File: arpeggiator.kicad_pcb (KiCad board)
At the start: 4 copper layers, 220 x 170 mm, 360 parts, among them J202 logic test header, J601 3.5mm mono line out, J701 PJ-102AH / 12V DC centre +, Q601 2N7002, Q602 MMBT3904, Q603 BSS84, Q604 MMBT3904, Q605 2N7002, Q606 MMBT3906, Q701 AO3401A, Q702 MMBT3906, Q703 MMBT3906, SW101 C, SW102 C sharp, SW103 D, SW104 D sharp, SW105 E, SW106 F, SW107 F sharp, SW108 G, SW109 G sharp, SW110 A, SW111 A sharp, SW112 B, SW113 start / stop, SW114 1 / 2 / 3 octaves, SW601 saw / pulse, U101 TLC555IDR, U102 TLC555IDR, U103 MCP100T-450I/TT, U201 74HC574, U202 74HC574, U203 74HC574, U204 74HC574, U205 74HC377, U206 74HC377, U211 74HC163, U212 74HC138, U213 74HC163, U214 74HC163, U215 74HC163, U216 CD74HC4067M, U221 74HC377, U222 74HC154, U301 74HC74, U302 74HC74, U303 74HC74, U401 74HC14, U402 74HC14, U403 74HC14, U404 74HC04, U405 74HC04, U406 74HC08, U407 74HC86, U408 74HC04, U409 74HC32, U410 74HC32, U411 74HC32, U412 74HC32, U413 74HC08, U414 74HC08, U415 74HC86, U416 74HC04, U417 74HC08, U418 74HC08, U419 74HC32, U420 74HC14, U421 74HC08, U422 74HC32, U423 74HC08, U424 74HC32, U425 74HC08, U501 OPA4192IDR, U502 ADG706BRUZ, U503 74HC4051D, U504 AS3340A, U601 TLC555IDR, U602 OPA4192IDR, U603 TL074HIDR, U604 LM13700M/NOPB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

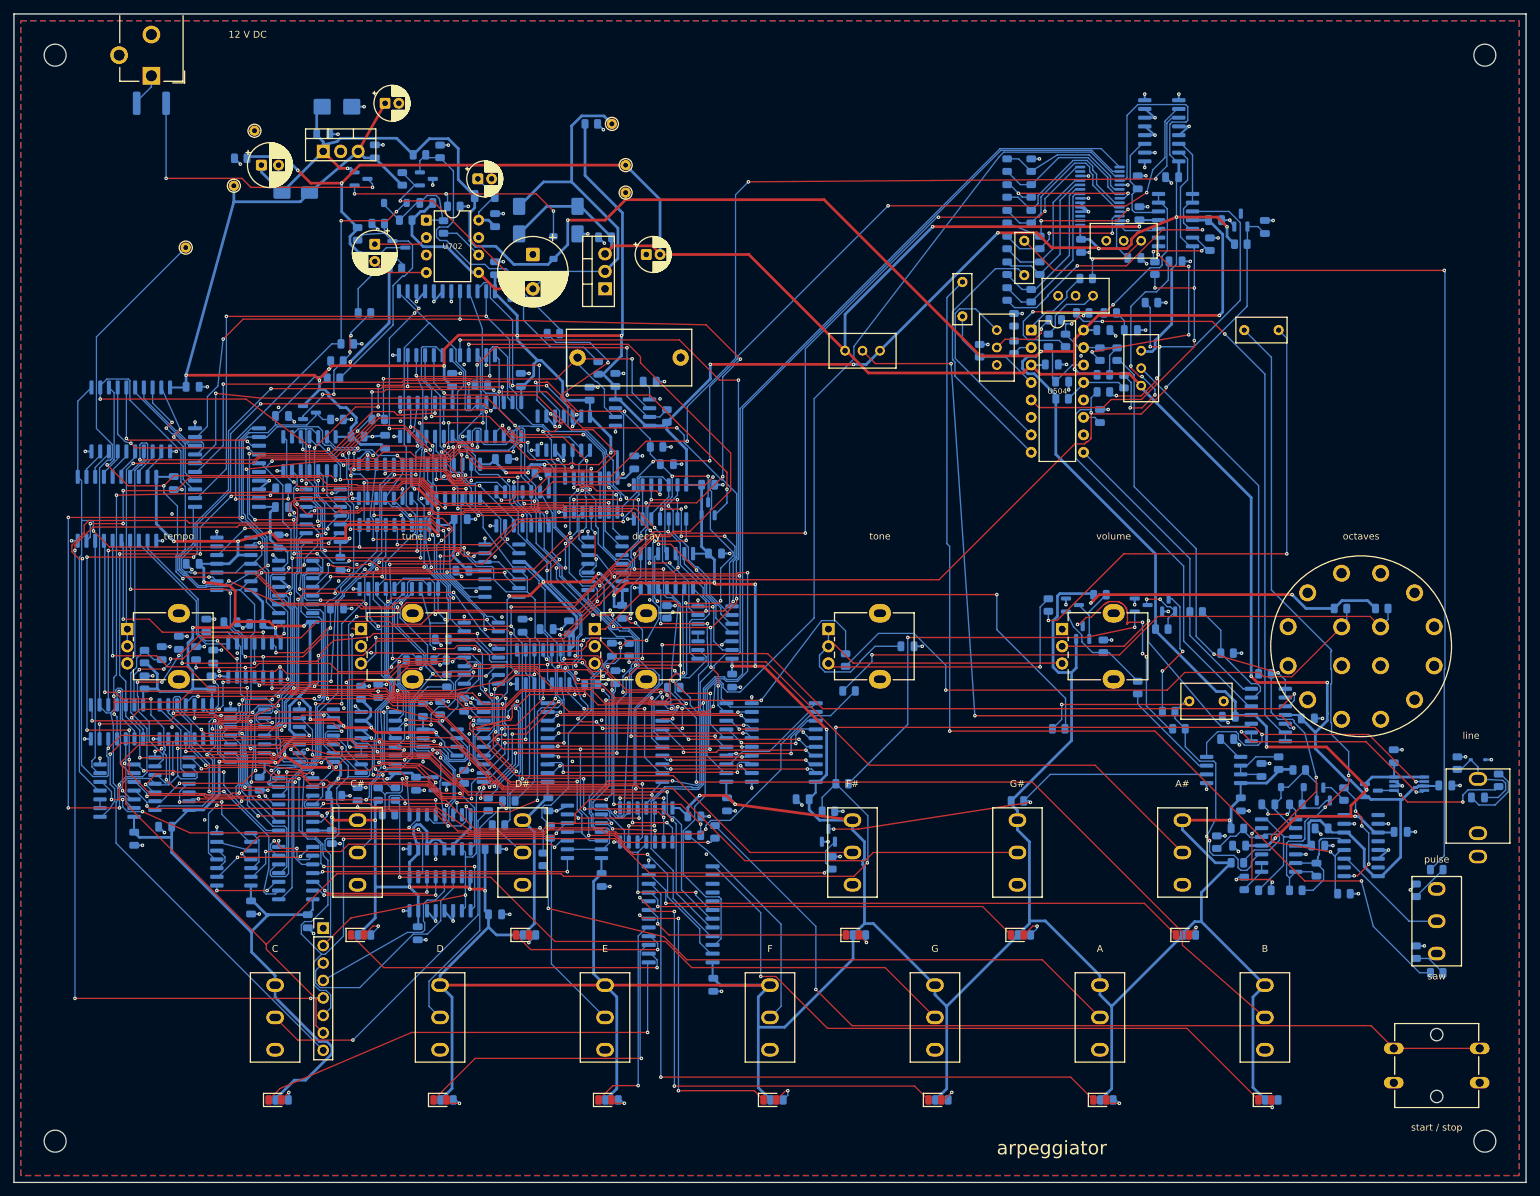
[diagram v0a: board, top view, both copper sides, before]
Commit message: parts and cheaper PCB files
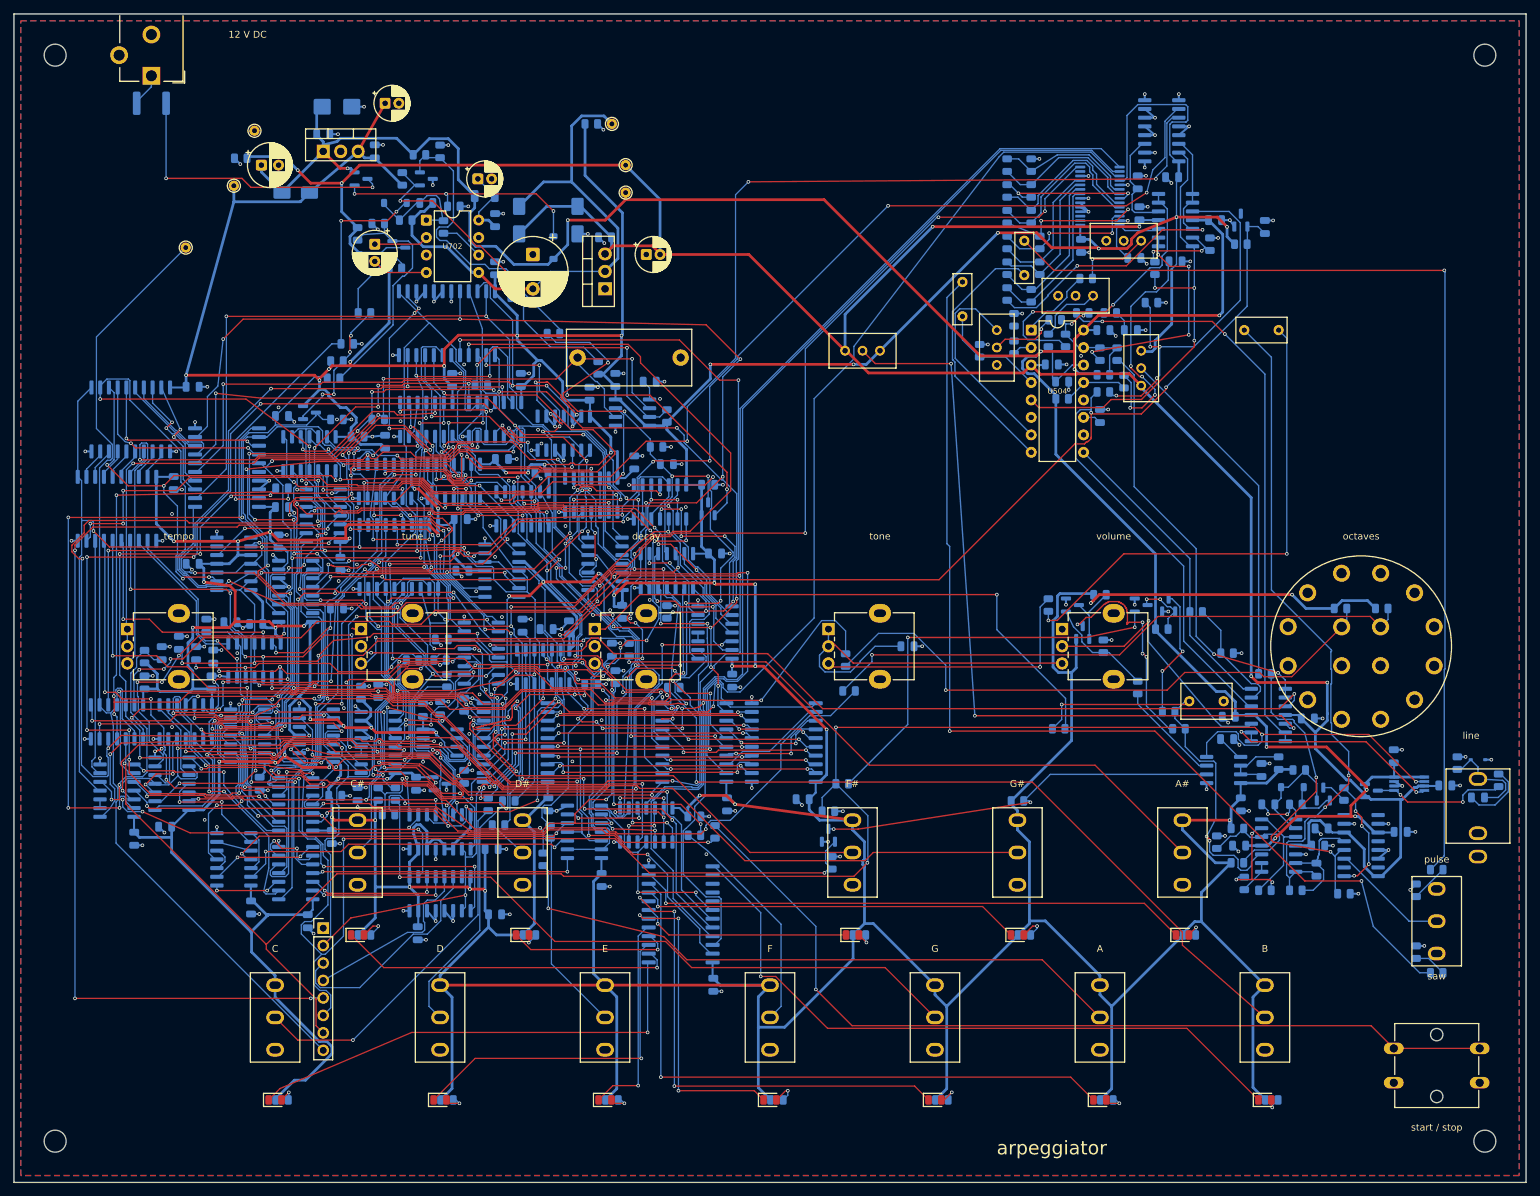
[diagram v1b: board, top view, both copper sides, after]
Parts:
- F701: value MF-MSMF025-2 / 250mA -> MF-MSMF035/33X-2 / 350mA
- U705: value TMUX6219DGKR -> TMUX6219DGKRQ1
